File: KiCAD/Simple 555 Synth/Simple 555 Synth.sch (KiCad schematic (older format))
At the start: 10 parts, among them P1 PWR_5v, P4 EasyLAB_LOGO, U1 555-timer, U2 555-timer

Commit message: Schema Versie 20180618 0.4
LM358 OpAmp toegevoegd
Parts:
- removed P1: PWR_5v, Socket_Strips:Socket_Strip_Angled_1x02, symbol CONN_01X02
- removed R2: R1k, w_pth_resistors:RC07, symbol R
- removed U1, U2: 555-timer, w_pth_circuits:dil_8-300_socket, symbol TLC555
- added C2: 10uF, symbol CP1_Small
- added D1: LED1, symbol LED_Small_ALT
- added J1: Stroom, symbol Conn_01x02
- added J2: CapacitorInput, symbol Conn_01x02
- added R2, R5: R_PHOTO1, symbol R_PHOTO
- added R4: R470K, symbol R
- added R6, R7: R1K, symbol R
- added RV1: POT, symbol POT
- added U1, U2: NE555, symbol NE555
- added U3: LM358, symbol LM358
- C1: value 01.uF -> 0.1uF; footprint Capacitors_ThroughHole:C_Disc_D3_P2.5 -> (none)
- C3: footprint Capacitors_ThroughHole:C_Radial_D6.3_L11.2_P2.5 -> (none)
- R1: value R100k -> R470K; footprint w_pth_resistors:RC07 -> (none)
- R3: value R50k -> 220; footprint w_pth_resistors:RC07 -> (none)
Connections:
- net labels added: Cap+, RST1, RST2, THR1, TRG1, geluid1, geluid2
- net labels removed: DIS, DIS2, OUT, RESET, RESET2, SPKR, THR, THR2, TRG, TRG2
- wire segments 37 -> 53
- no-connect marks 5 -> 4
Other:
- note added: "OpAmp"
- note added: "Oscilator1"
- note added: "Oscilator2"
- note added: "https://youtu.be/LbVDpv5OEf4?t=947"
- moved on the sheet: P4, SP1

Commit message: schema en printplaat Versie 20180625 0.6
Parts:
- removed SP1: Luidspreker, Buzzers_Beepers:Buzzer_12x9.5RM7.6, symbol SPEAKER
- added D2: LED2, LEDs:LED_D3.0mm, symbol LED_Small_ALT
- added J3: geluid_uit, footprints:Tayda_3.5mm_stereo_TRS_jack_A-853, symbol Audio-Jack-5
- added R8: R1k, w_pth_resistors:RC07, symbol R
- C1, C2, C3: footprint (none) -> Capacitors_ThroughHole:C_Radial_D5_L11_P2.5
- D1: footprint (none) -> LEDs:LED_D3.0mm
- J1: footprint (none) -> Socket_Strips:Socket_Strip_Angled_1x02
- J2: footprint (none) -> Socket_Strips:Socket_Strip_Straight_1x02
- P4: symbol CONN_01X01 -> Conn_01x01
- R1, R2, R4, R6, R7: footprint (none) -> w_pth_resistors:RC07
- R3: value 220 -> R1K; footprint (none) -> w_pth_resistors:RC07
- R5: value R_PHOTO1 -> R_PHOTO2; footprint (none) -> w_pth_resistors:RC07
- RV1: value POT -> POT_50k; footprint (none) -> w_pth_resistors:trimmer_ecp_ca9-v10
- U1, U2, U3: footprint (none) -> w_pth_circuits:dil_8-300_socket
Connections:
- net RST2: no longer RV1.3
- net TRG1: now also D1.1 (K), RV1.3, D2.1 (K), J3.5; no longer D1.2 (A)
- net at RV1.1: now also C3.2, R8.1
- net at RV1.2: now also J3.1, J3.2, J3.3, J3.4; no longer C3.2
- net at R3.2: now also D1.2 (A); no longer D1.1 (K)
- new net: D2.2 (A), R8.2
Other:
- moved on the sheet: D1, RV1

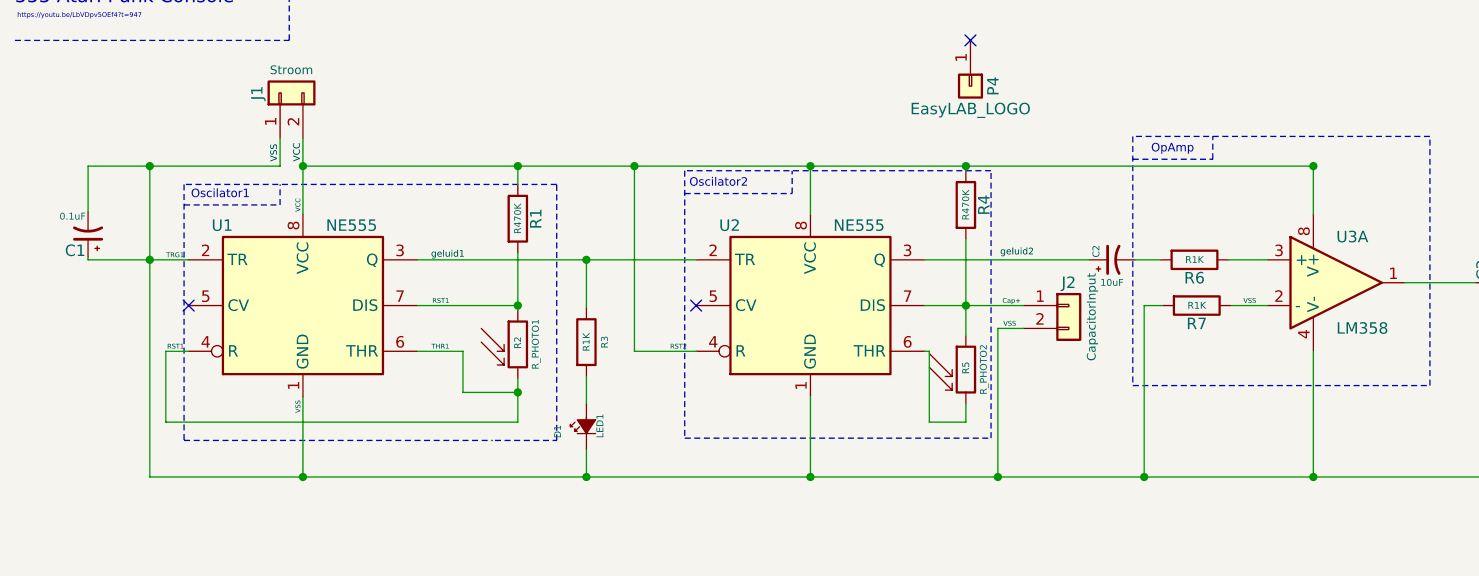
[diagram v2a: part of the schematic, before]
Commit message: Printplaat Versie 20180627 0.6
silkscreen teksten toegevoegd
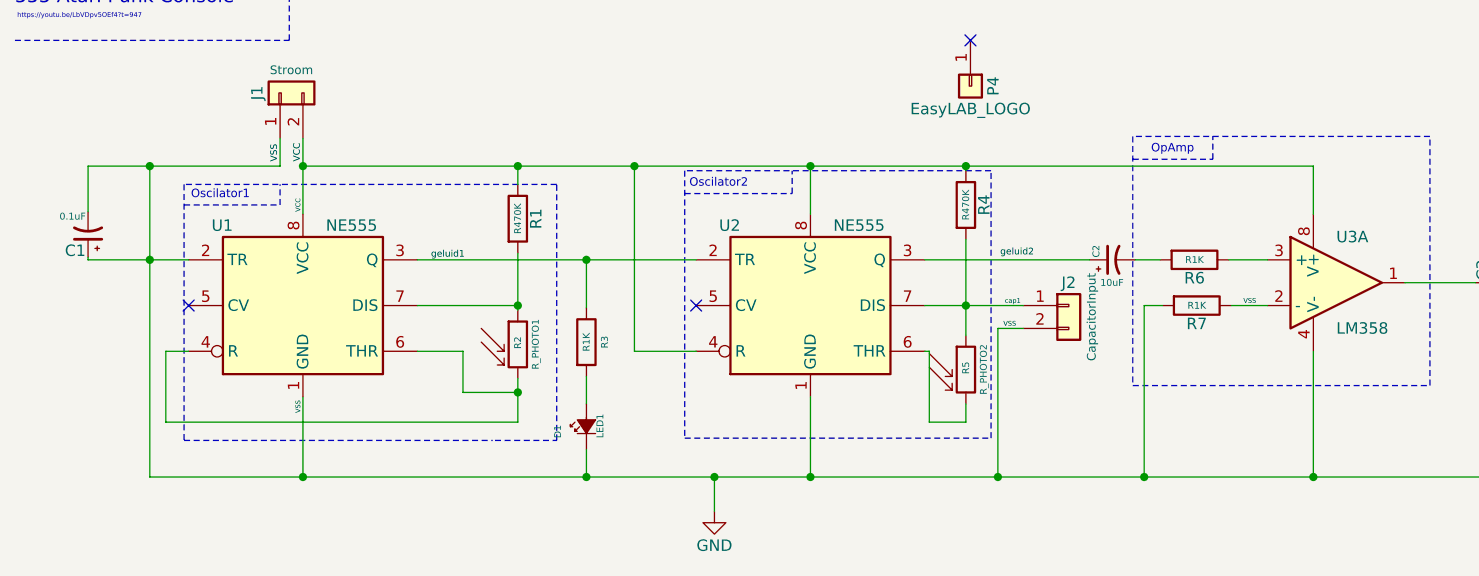
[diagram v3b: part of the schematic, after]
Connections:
- net Cap+ is gone; now on net cap1: J2.1 (Pin_1), R5.1, U2.7 (DIS)
- net cap1: now reaches R4.2
- net RST1: no longer names the net of R2.2, U1.4 (R), U1.6 (THR)
- net RST1: no longer R1.2, R2.1, U1.7 (DIS)
- net RST2 renamed VCC
- net TRG1 renamed GND
- new net: R1.2, R2.1, U1.7 (DIS)
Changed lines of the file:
@@
 Sheet 1 1
 Title "555 Atari Punk Console"
-Date "2018-06-25"
+Date "2018-06-28"
 Rev "0.4"
 Comp "EasyLab4Kids"
-Comment1 "Versie 20180625 0.6"
+Comment1 "Versie 20180628 0.6"
 Comment2 ""
 Comment3 "http://easylab4kids.nl"
@@
 Text Notes 510  760  0    21   ~ 0
 https://youtu.be/LbVDpv5OEf4?t=947
-Text Label 1240 1810 2    21   ~ 0
-TRG1
 $Comp
 L Conn_01x02 J2
@@
 VSS
 Text Label 4900 2010 2    21   ~ 0
-Cap+
+cap1
 NoConn ~ 3480 2010
 $Comp
@@
 	1    0    0    -1
 $EndComp
-Text Label 1240 2210 2    21   ~ 0
-RST1
-Text Label 2400 2010 2    21   ~ 0
-RST1
-Text Label 2400 2210 2    21   ~ 0
-THR1
-Text Label 3440 2210 2    21   ~ 0
-RST2
 $Comp
 L LM358 U3
@@
 	2260 1810 3480 1810
 Wire Wire Line
-	1760 2410 1760 2760
-Wire Wire Line
 	1660 1400 1660 1280
 Wire Wire Line
@@
 Wire Wire Line
 	3980 2760 3980 2410
-Connection ~ 1760 2760
 Wire Wire Line
 	4910 2110 4800 2110
@@
 	4800 2110 4800 2760
 Connection ~ 3980 2760
-Connection ~ 4660 2010
 Wire Wire Line
 	3980 1400 3980 1610
@@
 	4660 1400 4660 1420
 Connection ~ 3980 1400
-Wire Wire Line
-	4660 1720 4660 2000
 Connection ~ 3210 1400
 Wire Wire Line
@@
 Connection ~ 4800 2760
 Wire Wire Line
-	6180 1400 6180 1610
-Wire Wire Line
 	6180 2760 6180 2210
 Wire Wire Line
@@
 Connection ~ 3000 2760
 Wire Wire Line
-	4660 2010 4660 2140
-Wire Wire Line
 	4480 2210 4500 2210
 Wire Wire Line
@@
 Wire Notes Line
 	5740 1370 5740 1270
-Connection ~ 6180 1400
 Wire Notes Line
 	3550 1420 3430 1420
@@
 Wire Wire Line
 	1760 1280 1760 1610
+Wire Wire Line
+	6180 1400 6180 1610
+Wire Wire Line
+	4660 1720 4660 2140
+Connection ~ 4660 2010
+Wire Wire Line
+	1760 2410 1760 2760
+Connection ~ 1760 2760
+$Comp
+L GND #PWR01
+U 1 1 5B354FF7
+P 3560 2910
+F 0 "#PWR01" H 3560 2660 50  0001 C CNN
+F 1 "GND" H 3560 2760 50  0000 C CNN
+F 2 "" H 3560 2910 50  0001 C CNN
+F 3 "" H 3560 2910 50  0001 C CNN
+	1    3560 2910
+	1    0    0    -1
+$EndComp
+Wire Wire Line
+	3560 2910 3560 2760
+Connection ~ 3560 2760
 $EndSCHEMATC
